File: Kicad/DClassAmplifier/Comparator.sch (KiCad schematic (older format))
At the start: 4 parts, among them U5 LM319

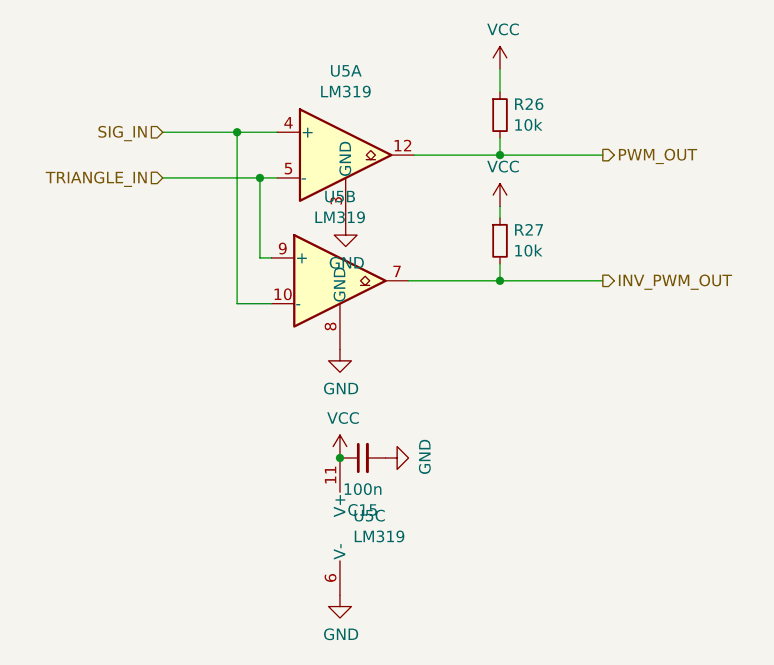
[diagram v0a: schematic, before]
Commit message: Add 10V Reg and Reroute
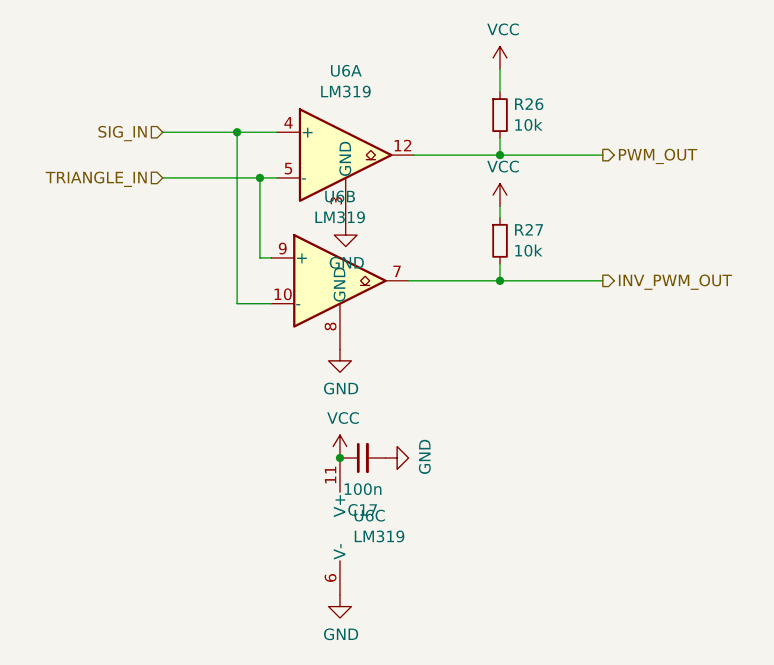
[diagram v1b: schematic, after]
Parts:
- renumbered C15 to C17, U5 to U6
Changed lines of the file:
@@
 $EndDescr
 $Comp
-L Comparator:LM319 U5
+L Comparator:LM319 U6
 U 1 1 61116116
 P 5150 2875
-F 0 "U5" H 5150 3242 50  0000 C CNN
+F 0 "U6" H 5150 3242 50  0000 C CNN
 F 1 "LM319" H 5150 3151 50  0000 C CNN
 F 2 "Package_SO:SO-14_3.9x8.65mm_P1.27mm" H 5150 2875 50  0001 C CNN
@@
 $EndComp
 $Comp
-L Comparator:LM319 U5
+L Comparator:LM319 U6
 U 2 1 6111611C
 P 5125 3425
-F 0 "U5" H 5125 3792 50  0000 C CNN
+F 0 "U6" H 5125 3792 50  0000 C CNN
 F 1 "LM319" H 5125 3701 50  0000 C CNN
 F 2 "Package_SO:SO-14_3.9x8.65mm_P1.27mm" H 5125 3425 50  0001 C CNN
@@
 $EndComp
 $Comp
-L Comparator:LM319 U5
+L Comparator:LM319 U6
 U 3 1 61116122
 P 5225 4500
-F 0 "U5" H 5183 4546 50  0000 L CNN
+F 0 "U6" H 5183 4546 50  0000 L CNN
 F 1 "LM319" H 5183 4455 50  0000 L CNN
 F 2 "Package_SO:SO-14_3.9x8.65mm_P1.27mm" H 5225 4500 50  0001 C CNN
@@
 	4675 3525 4825 3525
 $Comp
-L power:GND #PWR044
+L power:GND #PWR047
 U 1 1 61116132
 P 5150 3175
-F 0 "#PWR044" H 5150 2925 50  0001 C CNN
+F 0 "#PWR047" H 5150 2925 50  0001 C CNN
 F 1 "GND" H 5155 3002 50  0000 C CNN
 F 2 "" H 5150 3175 50  0001 C CNN
@@
 $EndComp
 $Comp
-L power:GND #PWR045
+L power:GND #PWR048
 U 1 1 61116138
 P 5125 3725
-F 0 "#PWR045" H 5125 3475 50  0001 C CNN
+F 0 "#PWR048" H 5125 3475 50  0001 C CNN
 F 1 "GND" H 5130 3552 50  0000 C CNN
 F 2 "" H 5125 3725 50  0001 C CNN
@@
 $EndComp
 $Comp
-L power:GND #PWR048
+L power:GND #PWR051
 U 1 1 6111613E
 P 5125 4800
-F 0 "#PWR048" H 5125 4550 50  0001 C CNN
+F 0 "#PWR051" H 5125 4550 50  0001 C CNN
 F 1 "GND" H 5130 4627 50  0000 C CNN
 F 2 "" H 5125 4800 50  0001 C CNN
@@
 $EndComp
 $Comp
-L power:VCC #PWR046
+L power:VCC #PWR049
 U 1 1 61116144
 P 5125 4200
-F 0 "#PWR046" H 5125 4050 50  0001 C CNN
+F 0 "#PWR049" H 5125 4050 50  0001 C CNN
 F 1 "VCC" H 5140 4373 50  0000 C CNN
 F 2 "" H 5125 4200 50  0001 C CNN
@@
 $EndComp
 $Comp
-L power:VCC #PWR042
+L power:VCC #PWR045
 U 1 1 6111A8CA
 P 5825 2500
-F 0 "#PWR042" H 5825 2350 50  0001 C CNN
+F 0 "#PWR045" H 5825 2350 50  0001 C CNN
 F 1 "VCC" H 5840 2673 50  0000 C CNN
 F 2 "" H 5825 2500 50  0001 C CNN
@@
 $EndComp
 $Comp
-L power:VCC #PWR043
+L power:VCC #PWR046
 U 1 1 6111AE94
 P 5825 3100
-F 0 "#PWR043" H 5825 2950 50  0001 C CNN
+F 0 "#PWR046" H 5825 2950 50  0001 C CNN
 F 1 "VCC" H 5840 3273 50  0000 C CNN
 F 2 "" H 5825 3100 50  0001 C CNN
@@
 AR Path="/610C616D/611DC342" Ref="C?"  Part="1"
 AR Path="/611D4178/611DC342" Ref="C?"  Part="1"
-AR Path="/61113C55/611DC342" Ref="C15"  Part="1"
-F 0 "C15" V 4996 4200 50  0000 C CNN
+AR Path="/61113C55/611DC342" Ref="C17"  Part="1"
+F 0 "C17" V 4996 4200 50  0000 C CNN
 F 1 "100n" V 5087 4200 50  0000 C CNN
 F 2 "Capacitor_SMD:C_0603_1608Metric_Pad1.08x0.95mm_HandSolder" H 5225 4200 50  0001 C CNN
@@
 $EndComp
 $Comp
-L power:GND #PWR047
+L power:GND #PWR050
 U 1 1 611DC348
 P 5325 4200
-F 0 "#PWR047" H 5325 3950 50  0001 C CNN
+F 0 "#PWR050" H 5325 3950 50  0001 C CNN
 F 1 "GND" H 5330 4027 50  0000 C CNN
 F 2 "" H 5325 4200 50  0001 C CNN
